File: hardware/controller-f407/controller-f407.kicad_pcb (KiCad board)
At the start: 2 copper layers, 159 x 99 mm, 124 parts, among them J1 AC_PIGTAIL, J2 CDE_1to8, J3 SWD, J4 UART, J5 EL_POT, K1 G5LE-1A4-DC5, Q1 AO3400A, Q2 BTA16-600SWRG, Q3 2N7002, Q4 BTA16-600SWRG, Q5 2N7002, Q6 BTA16-600SWRG, Q7 2N7002, U1 LTV-814S-TA1, U2 MOC3023SM, U3 LTV-814S-TA1, U4 MOC3023SM, U5 LTV-814S-TA1, U6 MOC3023SM, U7 LTV-814S-TA1, U8 STM32G431RBTx

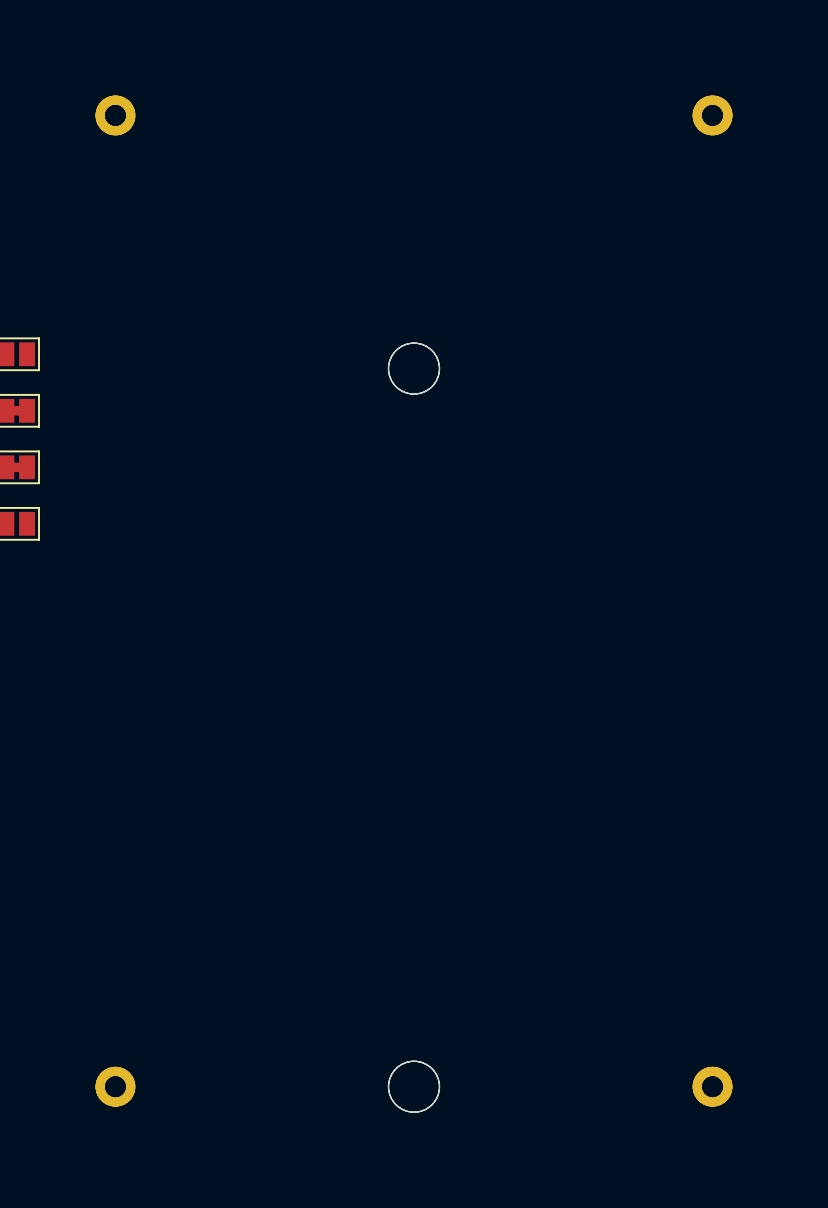
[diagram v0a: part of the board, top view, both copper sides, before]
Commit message: Remove the placeholder motor-cap footprints that sat on C6 and C7. (#13)
C_MOTOR1 and C_MOTOR2 had no nets and overlapped the real run capacitors, which produced clearance, solder-mask, and co-located-hole DRC hits. HS1, the aluminum heat bar, is mechanical: mark it not in the schematic and keep it out of the BOM and position files.

Co-authored-by: Cursor Agent <cursoragent@cursor.com>
Co-authored-by: Jeffrey Millar <wa1hco@users.noreply.github.com>
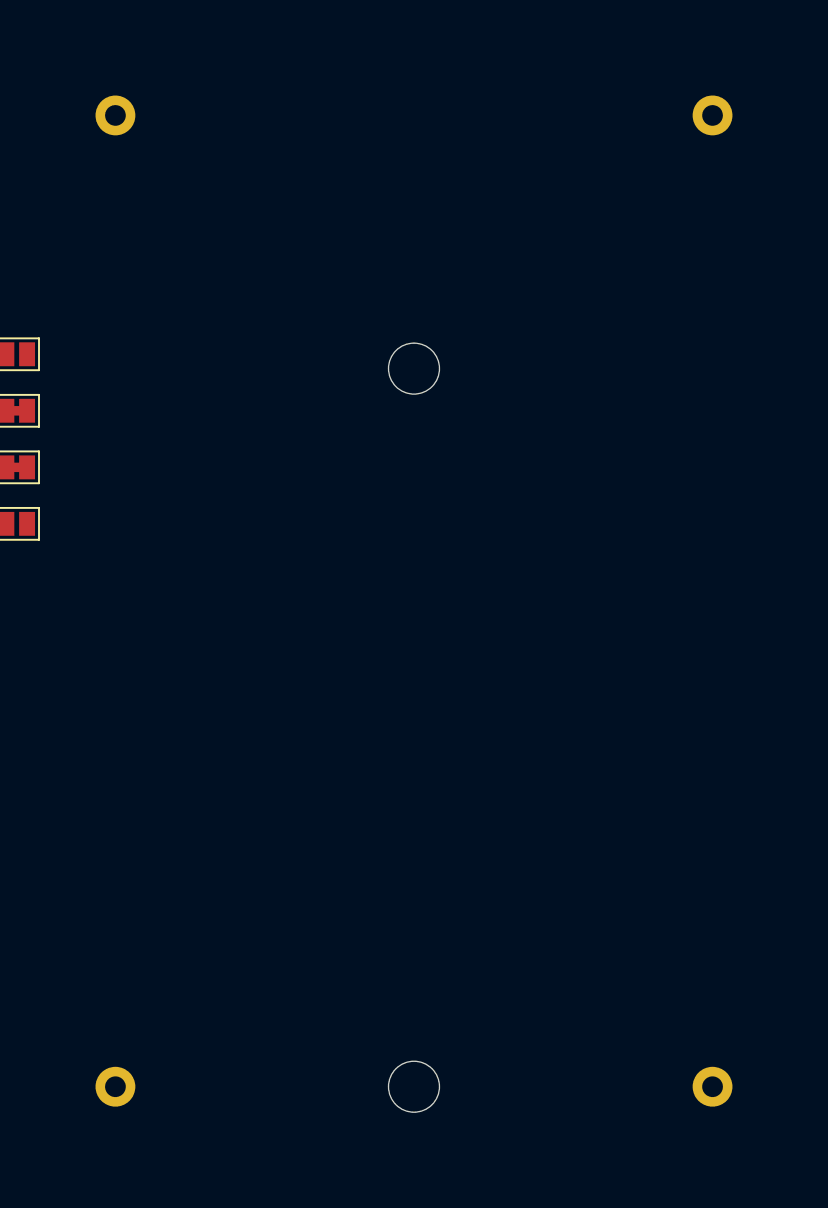
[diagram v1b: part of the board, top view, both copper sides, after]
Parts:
- removed C_MOTOR1: R60EW61005000K, C_Rect_KEMET_R60_P37.5_L41.5_W20_H40_Flat
- removed C_MOTOR2: B32526T1336K000, C_Rect_TDK_B32526T_P37.5_L41.5_W24_H15_Upright
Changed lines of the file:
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@@
 	(net 112 "unconnected-(U8-PA15-Pad51)")
 	(net 113 "unconnected-(U8-PA9-Pad43)")
-	(footprint "C_Rect_TDK_B32526T_P37.5_L41.5_W24_H15_Upright"
-		(layer "F.Cu")
-		(at 259.51 80.06 90)
-		(property "Reference" "C_MOTOR2"
-			(at 0 0 90)
-			(layer "F.SilkS")
-			(hide yes)
-			(effects
-				(font
-					(size 1.27 1.27)
-					(thickness 0.15)
-				)
-			)
-		)
-		(property "Value" "B32526T1336K000"
-			(at 0 0 90)
-			(layer "F.Fab")
-			(hide yes)
-			(effects
-				(font
-					(size 1.27 1.27)
-					(thickness 0.15)
-				)
-			)
-		)
-		(property "Datasheet" ""
-			(at 0 0 90)
-			(layer "F.Fab")
-			(hide yes)
-			(effects
-				(font
-					(size 1.27 1.27)
-					(thickness 0.15)
-				)
-			)
-		)
-		(property "Description" ""
-			(at 0 0 90)
-			(layer "F.Fab")
-			(hide yes)
-			(effects
-				(font
-					(size 1.27 1.27)
-					(thickness 0.15)
-				)
-			)
-		)
-		(pad "1" thru_hole circle
-			(at 0 0 90)
-			(size 2.5 2.5)
-			(drill 1.3)
-			(layers "*.Cu" "*.Mask")
-			(remove_unused_layers no)
-		)
-		(pad "2" thru_hole circle
-			(at 0 37.5 90)
-			(size 2.5 2.5)
-			(drill 1.3)
-			(layers "*.Cu" "*.Mask")
-			(remove_unused_layers no)
-		)
-		(embedded_fonts no)
-	)
 	(footprint "AL_BAR_10x50"
 		(layer "F.Cu")
@@
 			)
 		)
-		(attr exclude_from_pos_files exclude_from_bom)
+		(attr board_only exclude_from_pos_files exclude_from_bom)
 		(pad "" np_thru_hole circle
 			(at 0 -20)
@@
 		)
 	)
-	(footprint "C_Rect_KEMET_R60_P37.5_L41.5_W20_H40_Flat"
-		(layer "F.Cu")
-		(at 259.51 141.06 90)
-		(property "Reference" "C_MOTOR1"
-			(at 0 0 90)
-			(layer "F.SilkS")
-			(hide yes)
-			(effects
-				(font
-					(size 1.27 1.27)
-					(thickness 0.15)
-				)
-			)
-		)
-		(property "Value" "R60EW61005000K"
-			(at 0 0 90)
-			(layer "F.Fab")
-			(hide yes)
-			(effects
-				(font
-					(size 1.27 1.27)
-					(thickness 0.15)
-				)
-			)
-		)
-		(property "Datasheet" ""
-			(at 0 0 90)
-			(layer "F.Fab")
-			(hide yes)
-			(effects
-				(font
-					(size 1.27 1.27)
-					(thickness 0.15)
-				)
-			)
-		)
-		(property "Description" ""
-			(at 0 0 90)
-			(layer "F.Fab")
-			(hide yes)
-			(effects
-				(font
-					(size 1.27 1.27)
-					(thickness 0.15)
-				)
-			)
-		)
-		(pad "" np_thru_hole circle
-			(at 0 18.75 90)
-			(size 3.2 3.2)
-			(drill 3.2)
-			(layers "*.Cu" "*.Mask")
-		)
-		(pad "" np_thru_hole circle
-			(at 45.1 18.75 90)
-			(size 3.2 3.2)
-			(drill 3.2)
-			(layers "*.Cu" "*.Mask")
-		)
-		(pad "1" thru_hole circle
-			(at 0 0 90)
-			(size 2.5 2.5)
-			(drill 1.3)
-			(layers "*.Cu" "*.Mask")
-			(remove_unused_layers no)
-		)
-		(pad "2" thru_hole circle
-			(at 0 37.5 90)
-			(size 2.5 2.5)
-			(drill 1.3)
-			(layers "*.Cu" "*.Mask")
-			(remove_unused_layers no)
-		)
-		(embedded_fonts no)
-	)
 	(footprint "Resistor_SMD:R_0603_1608Metric"
